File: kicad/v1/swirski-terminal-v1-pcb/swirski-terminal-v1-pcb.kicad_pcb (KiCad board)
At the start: 2 copper layers, 28 parts, among them J1 Conn_01x07_Pin, Q2 PN2222A, Q3 BC327, SW1 RotaryEncoder_Switch, SW2 SW_Home, SW3 SW_Back, U1 Seeed_Lipo_Rider_Plus, U2 Adafruit_MAX17048, U3 ESP32_S3_Super_Mini, U4 MCP23008-xSO, U5 ILI9341_DEV

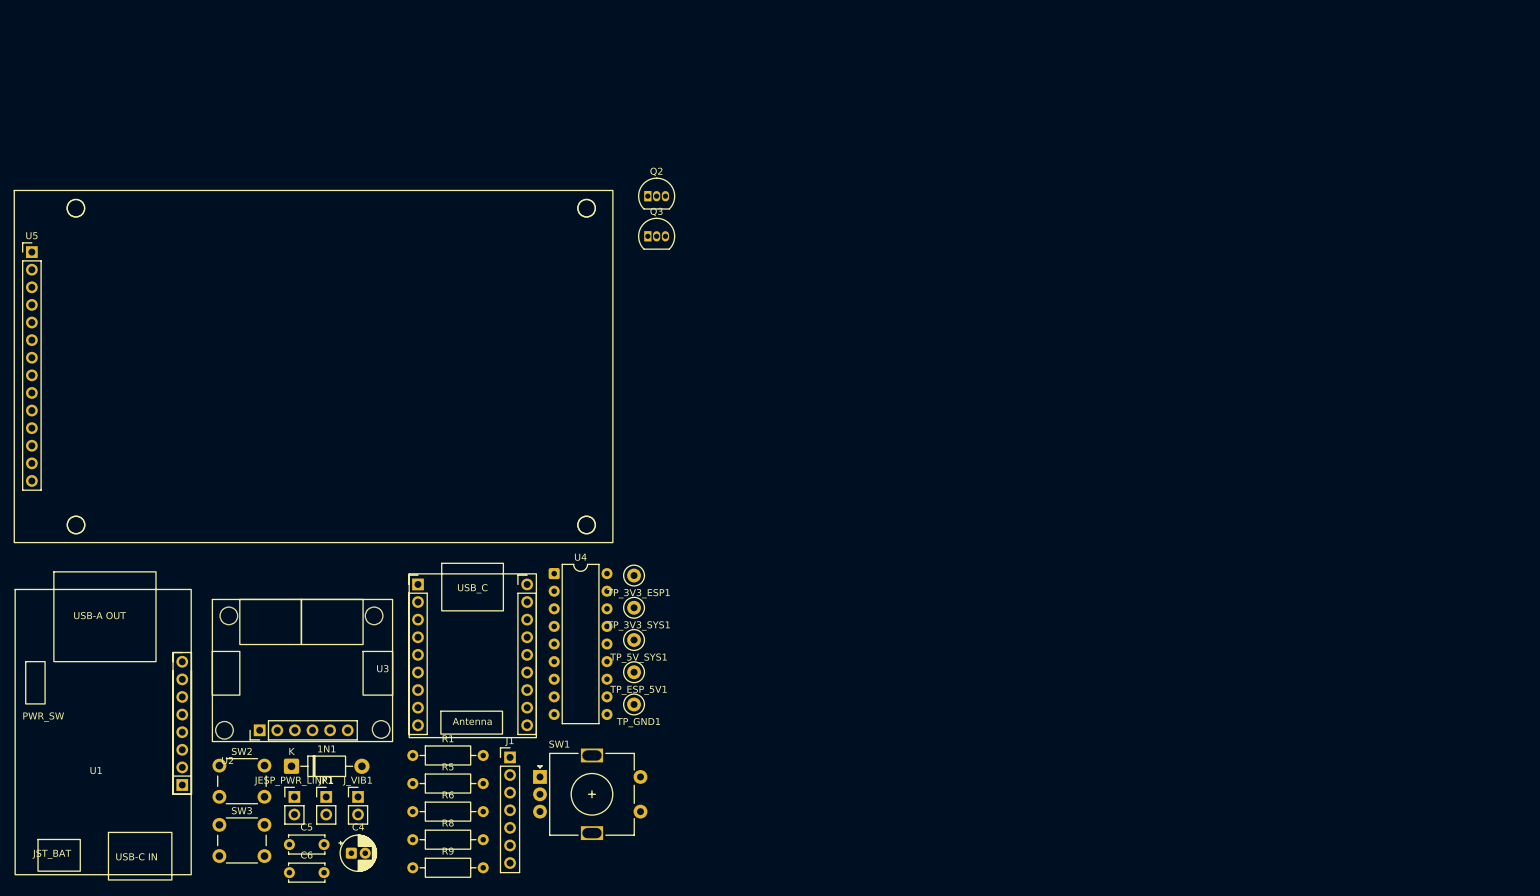
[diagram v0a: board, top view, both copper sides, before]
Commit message: Add lock file for KiCad schematic to prevent concurrent edits
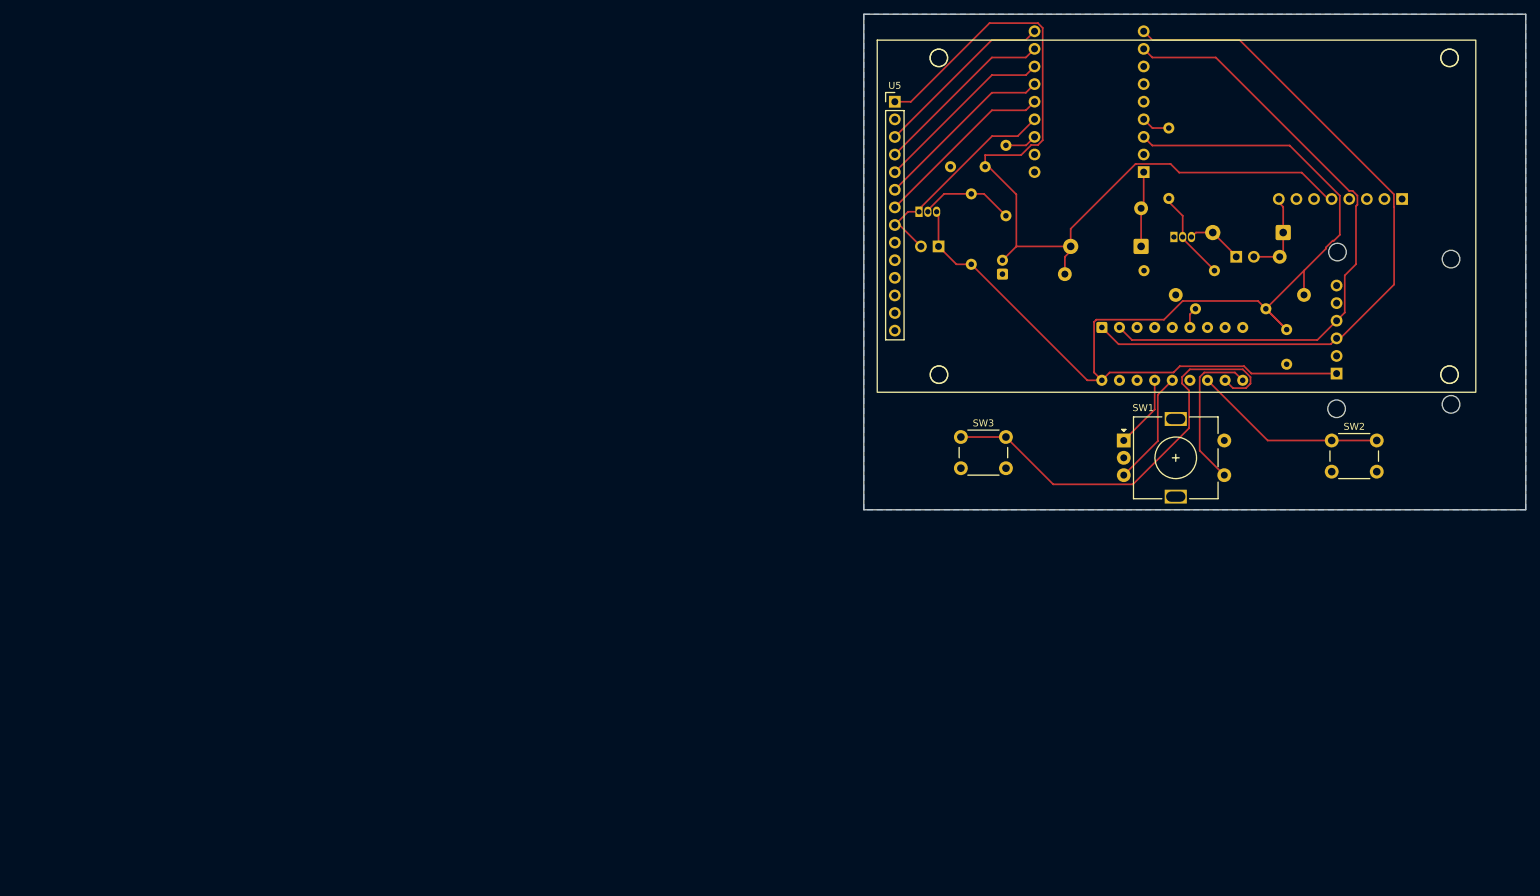
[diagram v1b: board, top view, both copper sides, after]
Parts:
- removed 1N1: 1N5819, Diode_THT:D_DO-41_SOD81_P10.16mm_Horizontal
- removed J1: Conn_01x07_Pin, Connector_PinHeader_2.54mm:PinHeader_1x07_P2.54mm_Vertical
- removed JESP_PWR_LINK1: Conn_01x02_Pin, Connector_PinHeader_2.54mm:PinHeader_1x02_P2.54mm_Vertical
- added D1: 1N5819, Diode_THT:D_DO-41_SOD81_P10.16mm_Horizontal, B.Cu at (226.5, 54.0)
- added D2: 1N5819, Diode_THT:D_DO-41_SOD81_P10.16mm_Horizontal, B.Cu at (247.0, 52.0)
- C4, C5, C6, JP1, J_VIB1, Q2, Q3, R1, R5, R6, R8, R9, TP_3V3_ESP1, TP_3V3_SYS1, TP_5V_SYS1, TP_ESP_5V1, TP_GND1, U1, U2, U3: moved to B.Cu
- U4: value MCP23008-xSO -> MCP23008-E/P; moved to B.Cu
- moved U1 171.7 mm to (246.4, 47.2), turned to -90 degrees
- moved SW2 167.2 mm to (254.0, 82.0)
- moved C6 163.8 mm to (247.5, 66.0), turned to -90 degrees
- moved U2 163.7 mm to (254.7, 72.3), turned to 90 degrees
- moved J_VIB1 148.7 mm to (240.2, 55.5), turned to -90 degrees
- moved R6 147.1 mm to (230.5, 36.9), turned to -90 degrees
- moved R5 140.9 mm to (244.5, 63.0), turned to 180 degrees
- moved C5 136.6 mm to (199.0, 42.5)
- moved R9 136.2 mm to (226.9, 57.5)
- moved U5 126.4 mm to (191.0, 33.1)
- moved C4 125.7 mm to (206.5, 58.0), turned to 90 degrees
- moved R1 122.8 mm to (207.0, 39.4), turned to -90 degrees
- moved SW3 120.7 mm to (200.5, 81.5)
- moved JP1 118.8 mm to (197.3, 54.0), turned to 90 degrees
- moved R8 115.7 mm to (202.0, 56.6), turned to 90 degrees
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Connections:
- U2 pad 1: /3V3_SYS -> /3V3_ESP
- U3 pad 10: /LCD_PIN_RST -> /I2C_SCL
- U3 pad 11: /ESP_SPARE_A -> /I2C_SDA
- U3 pad 12: /ENC_B -> unconnected-(U3-GPIO10-Pad12)
- U3 pad 13: /ENC_A -> unconnected-(U3-GPIO11-Pad13)
- U3 pad 14: /TFT_BL_PWM -> unconnected-(U3-GPIO12-Pad14)
- U3 pad 3: /I2C_SCL -> /TFT_BL_PWM
- U3 pad 4: /I2C_SDA -> /TFT LED PIN
- U3 pad 5: unconnected-(U3-GPIO3-Pad5) -> /LCD_PIN_SCLK
- U3 pad 6: /LCD_PIN_DC -> /LCD_PIN_MOSI
- U3 pad 7: /LCD_PIN_CS -> /LCD_PIN_DC
- U3 pad 8: /LCD_PIN_MOSI -> /LCD_PIN_RST
- U3 pad 9: /LCD_PIN_SCLK -> /LCD_PIN_CS
- U4 pad 14: unconnected-(U4-GP4-Pad14) -> /ENC_B
- U4 pad 15: unconnected-(U4-GP5-Pad15) -> /ENC_A
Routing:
- net /3V3_ESP: track 0.00 -> 171.8 mm
- net /5V_SYS: track 0.00 -> 127.2 mm
- net /I2C_SCL: track 0.00 -> 105.6 mm
- net /I2C_SDA: track 0.00 -> 92.1 mm
- net /BACK_BTN: track 0.00 -> 63.0 mm
- net /TFT LED PIN: track 0.00 -> 31.7 mm
- net /HOME_BTN: track 0.00 -> 28.0 mm
- net /LCD_PIN_SCLK: track 0.00 -> 26.5 mm
- net /LCD_PIN_RST: track 0.00 -> 26.5 mm
- net /LCD_PIN_MOSI: track 0.00 -> 26.5 mm
- net /LCD_PIN_DC: track 0.00 -> 26.5 mm
- net /LCD_PIN_CS: track 0.00 -> 26.5 mm
- net /ENC_SW: track 0.00 -> 22.6 mm
- net /ENC_B: track 0.00 -> 16.6 mm
- net Net-(Q3-B): track 0.00 -> 13.8 mm
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- added copper zone on B.Cu, net /GND
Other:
- board outline added: 95.5 x 71.5 mm
- board text added: "Wrist Terminal v1"
